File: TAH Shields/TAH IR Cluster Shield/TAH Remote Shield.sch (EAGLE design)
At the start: 12 parts, among them T1 2N3904

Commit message: TAH Shields new version update
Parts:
- R1, R2, R3, R4, R5: value (none) -> 1k
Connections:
- net D3: no longer R5.1
- net D9: now also R5.1
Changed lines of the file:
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@@
 <?xml version="1.0" encoding="utf-8"?>
 <!DOCTYPE eagle SYSTEM "eagle.dtd">
-<eagle version="6.4">
+<eagle version="7.0.0">
 <drawing>
 <settings>
@@
 <part name="LED3" library="1n4148 diode sot 23" deviceset="LED" device="5MM"/>
 <part name="LED4" library="1n4148 diode sot 23" deviceset="LED" device="5MM"/>
-<part name="R1" library="1n4148 diode sot 23" deviceset="R-US_" device="M1206"/>
-<part name="R2" library="1n4148 diode sot 23" deviceset="R-US_" device="M1206"/>
-<part name="R3" library="1n4148 diode sot 23" deviceset="R-US_" device="M1206"/>
-<part name="R4" library="1n4148 diode sot 23" deviceset="R-US_" device="M1206"/>
+<part name="R1" library="1n4148 diode sot 23" deviceset="R-US_" device="M1206" value="1k"/>
+<part name="R2" library="1n4148 diode sot 23" deviceset="R-US_" device="M1206" value="1k"/>
+<part name="R3" library="1n4148 diode sot 23" deviceset="R-US_" device="M1206" value="1k"/>
+<part name="R4" library="1n4148 diode sot 23" deviceset="R-US_" device="M1206" value="1k"/>
 <part name="GND" library="SparkFun-Aesthetics" deviceset="GND" device=""/>
-<part name="R5" library="1n4148 diode sot 23" deviceset="R-US_" device="M1206"/>
+<part name="R5" library="1n4148 diode sot 23" deviceset="R-US_" device="M1206" value="1k"/>
 <part name="RC1" library="Infrared Receiver TSOP" deviceset="PNA460XM" device=""/>
 </parts>
@@
 <net name="D3" class="0">
 <segment>
-<pinref part="R5" gate="G$1" pin="1"/>
-<wire x1="133.35" y1="104.14" x2="125.73" y2="104.14" width="0.1524" layer="91"/>
-<label x="125.73" y="104.14" size="1.778" layer="95"/>
-</segment>
-<segment>
 <pinref part="U$2" gate="G$1" pin="D3"/>
 <wire x1="73.66" y1="45.72" x2="85.09" y2="45.72" width="0.1524" layer="91"/>
@@
 <label x="77.47" y="76.2" size="1.778" layer="95"/>
 </segment>
-</net>
+<segment>
+<pinref part="R5" gate="G$1" pin="1"/>
+<wire x1="133.35" y1="104.14" x2="125.73" y2="104.14" width="0.1524" layer="91"/>
+<label x="125.73" y="104.14" size="1.778" layer="95"/>
+</segment>
+</net>

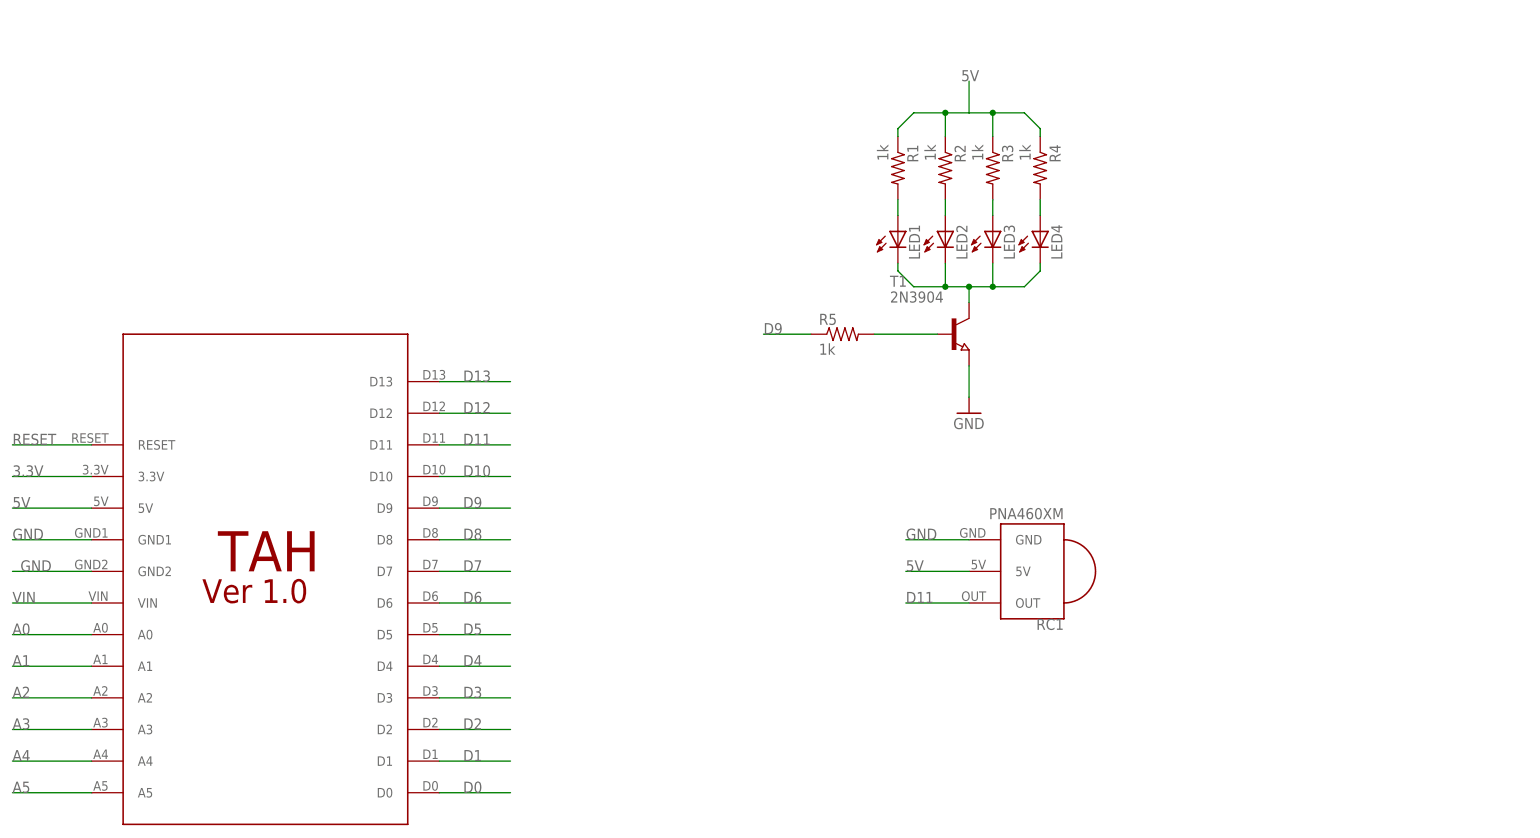
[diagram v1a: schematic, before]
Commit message: All shields updated with latest Tah footprint
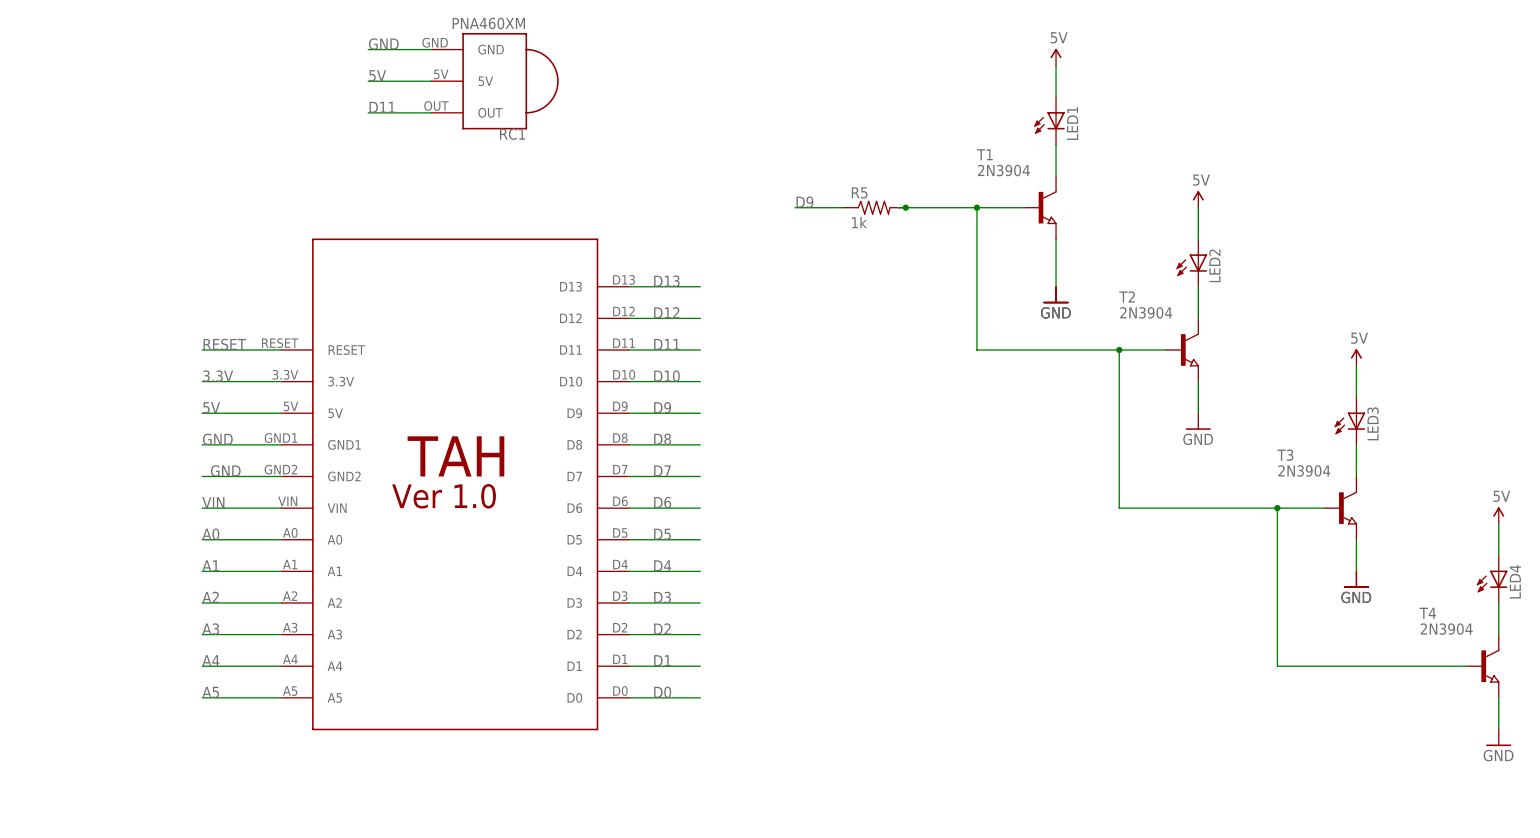
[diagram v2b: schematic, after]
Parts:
- removed R1, R2, R3, R4: 1k, 1n4148 diode sot 23:R-US_M1206
- added T2, T3, T4: 2N3904, semicon-smd-ipc:NPN-TRANSISTOR_SOT23
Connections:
- removed net N$6: R5.2, T1.B
- net 5V: now also LED1.A, LED2.A, LED3.A, LED4.A; no longer R1.1, R2.1, R3.1, R4.1
- net GND: now also T2.E, T3.E, T4.E
- net N$1: now also LED1.C, T1.C; no longer LED1.A, R1.2
- net N$2: now also LED2.C, T2.C; no longer LED2.A, R2.2
- net N$3: now also LED4.C, T4.C; no longer LED3.A, R3.2
- net N$4: now also LED3.C, T3.C; no longer LED4.A, R4.2
- net N$5: now also R5.2, T1.B, T2.B, T3.B, T4.B; no longer LED1.C, LED2.C, LED3.C, LED4.C, T1.C
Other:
- moved on the sheet: LED1, LED2, LED3, LED4, R5, RC1, T1
